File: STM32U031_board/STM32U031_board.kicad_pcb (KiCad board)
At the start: 2 copper layers, 4 parts, among them J3 SWD, J4 UART, J6 QT/ST, U1 STM32U031K8Ux

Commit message: Snapshot:
- after adding L1 inductor package
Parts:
- added C1: 0.1uF, Capacitor_SMD:C_0201_0603Metric, F.Cu at (53.5, 55.5)
- added C2: 47uF, Capacitor_SMD:C_1210_3225Metric, F.Cu at (60.5, 55.5)
- added J1: Conn_01x20, STM32U031_board:Pico_Header_1-20, F.Cu at (43.4, 64.4)
- added J2: Conn_01x20, STM32U031_board:Pico_Header_21-40, F.Cu at (43.4, 46.6)
- added J6: 3.6-15V in, Connector_JST:JST_PH_S2B-PH-SM4-TB_1x02-1MP_P2.00mm_Horizontal, F.Cu at (47.2, 55.5)
- added L1: 33uH, Inductor_SMD:L_Coilcraft_LPS4018, F.Cu at (56.5, 51.0)
- added U2: LTC3336EV#TRMPBF, STM32U031_board:LTC3336EVTRMPBF, F.Cu at (56.5, 55.5)
- J5: renamed from J6; footprint Connector_JST:JST_SH_BM04B-SRSS-TB_1x04-1MP_P1.00mm_Vertical -> Connector_JST:JST_SH_SM04B-SRSS-TB_1x04-1MP_P1.00mm_Horizontal
- moved J4 22.3 mm to (82.5, 51.5), turned to -90 degrees
- moved J3 13.9 mm to (82.5, 59.5), turned to -90 degrees
- moved U1 7.61 mm to (67.4, 55.5)
- moved J5 5.55 mm to (90.0, 55.5), turned to 90 degrees
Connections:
- U1 pad 10: /MCU/PA4 -> /Headers/PA4
- U1 pad 11: /MCU/PA5 -> /Headers/PA5
- U1 pad 12: /MCU/PA6 -> /Headers/PA6
- U1 pad 13: /MCU/PA7 -> /Headers/PA7
- U1 pad 14: /MCU/PB0 -> /Headers/PB0
- U1 pad 15: /MCU/PB1 -> /Headers/PB1
- U1 pad 18: /MCU/PA8 -> /Headers/PA8
- U1 pad 19: /MCU/PA9/TX -> /Connectors, LEDs, pushbutton/PA9/TX
- U1 pad 2: /MCU/PC14 -> /Headers/PC14
- U1 pad 20: /MCU/PA10/RX -> /Connectors, LEDs, pushbutton/PA10/RX
- U1 pad 21: /MCU/PA11 -> /Headers/PA11
- U1 pad 22: /MCU/PA12 -> /Headers/PA12
- U1 pad 23: /MCU/PA13/SWDIO -> /Connectors, LEDs, pushbutton/PA13/SWDIO
- U1 pad 24: /MCU/PA14/SWCLK -> /Connectors, LEDs, pushbutton/PA14/SWCLK
- U1 pad 25: /MCU/PA15 -> /Headers/PA15
- U1 pad 26: /MCU/PB3 -> /Headers/PB3
- U1 pad 27: /MCU/PB4 -> /Headers/PB4
- U1 pad 28: /MCU/PB5 -> /Headers/PB5
- U1 pad 29: /MCU/PB6/SCL -> /Connectors, LEDs, pushbutton/PB6/SCL
- U1 pad 3: /MCU/PC15 -> /Headers/PC15
- U1 pad 30: /MCU/PB7/SDA -> /Connectors, LEDs, pushbutton/PB7/SDA
- U1 pad 31: /MCU/PF3 -> /Connectors, LEDs, pushbutton/PF3
- U1 pad 4: /MCU/PF2 -> /Headers/PF2
- U1 pad 6: /MCU/PA0 -> /Headers/PA0
- U1 pad 7: /MCU/PA1 -> /Headers/PA1
- U1 pad 8: /MCU/PA2 -> /Headers/PA2
- U1 pad 9: /MCU/PA3 -> /Headers/PA3
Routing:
- net /Headers/PB0: track 0.00 -> 35.0 mm, vias 0 -> 4
- net /Headers/PB1: track 0.00 -> 31.9 mm, vias 0 -> 4
- net /Connectors, LEDs, pushbutton/PB7/SDA: track 0.00 -> 30.9 mm, vias 0 -> 1
- net /Connectors, LEDs, pushbutton/PB6/SCL: track 0.00 -> 29.6 mm, vias 0 -> 1
- net /Connectors, LEDs, pushbutton/PA14/SWCLK: track 0.00 -> 29.4 mm
- net /Headers/PA15: track 0.00 -> 28.8 mm
- net /Connectors, LEDs, pushbutton/PA10/RX: track 0.00 -> 26.6 mm, vias 0 -> 2
- net /Headers/PA0: track 0.00 -> 26.5 mm
- net /Connectors, LEDs, pushbutton/PA9/TX: track 0.00 -> 25.9 mm, vias 0 -> 2
- net /Headers/PA1: track 0.00 -> 24.0 mm
- net /Connectors, LEDs, pushbutton/PA13/SWDIO: track 0.00 -> 23.2 mm
- net /Headers/PA2: track 0.00 -> 19.0 mm
- net /Headers/PB3: track 0.00 -> 18.9 mm
- net /Headers/PB4: track 0.00 -> 16.9 mm
- net /Headers/PA12: track 0.00 -> 16.7 mm
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- added copper zone on B.Cu, net GND
- added copper zone on F.Cu, net GND
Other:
- board outline added: 51 x 21 mm

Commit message: Checkin prior to PSU change.
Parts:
- added C3: 100nF, Capacitor_SMD:C_0402_1005Metric, F.Cu at (65.1, 51.9)
- added C4: 100nF, Capacitor_SMD:C_0402_1005Metric, F.Cu at (69.7, 59.1)
- moved L1 0.50 mm to (57.0, 51.0)
- moved J5 0.35 mm to (89.7, 55.5)
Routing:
- net +3.3V: track 15.7 -> 70.3 mm, vias 0 -> 4
- net VSYS: track 0.00 -> 13.5 mm
- net Net-(U2-SW): track 0.00 -> 4.02 mm
- net /Headers/PF2: track 11.8 -> 15.1 mm
- net /Headers/PA12: track 16.7 -> 18.8 mm
- net /Connectors, LEDs, pushbutton/PA14/SWCLK: track 29.4 -> 30.4 mm
- net /Headers/PA15: track 28.8 -> 29.7 mm
- net /Connectors, LEDs, pushbutton/PB6/SCL: track 29.6 -> 30.5 mm
- net GND: track 10.4 -> 9.59 mm
- net /Connectors, LEDs, pushbutton/PA10/RX: track 26.6 -> 25.8 mm
- net /Connectors, LEDs, pushbutton/PB7/SDA: track 30.9 -> 31.5 mm
- net /Headers/PA11: track 14.0 -> 14.5 mm
- net /Headers/PA2: track 19.0 -> 19.1 mm, vias 0 -> 1
- net /Headers/PA0: track 26.5 -> 26.6 mm, vias 0 -> 1
- net /Headers/PA1: vias 0 -> 1
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
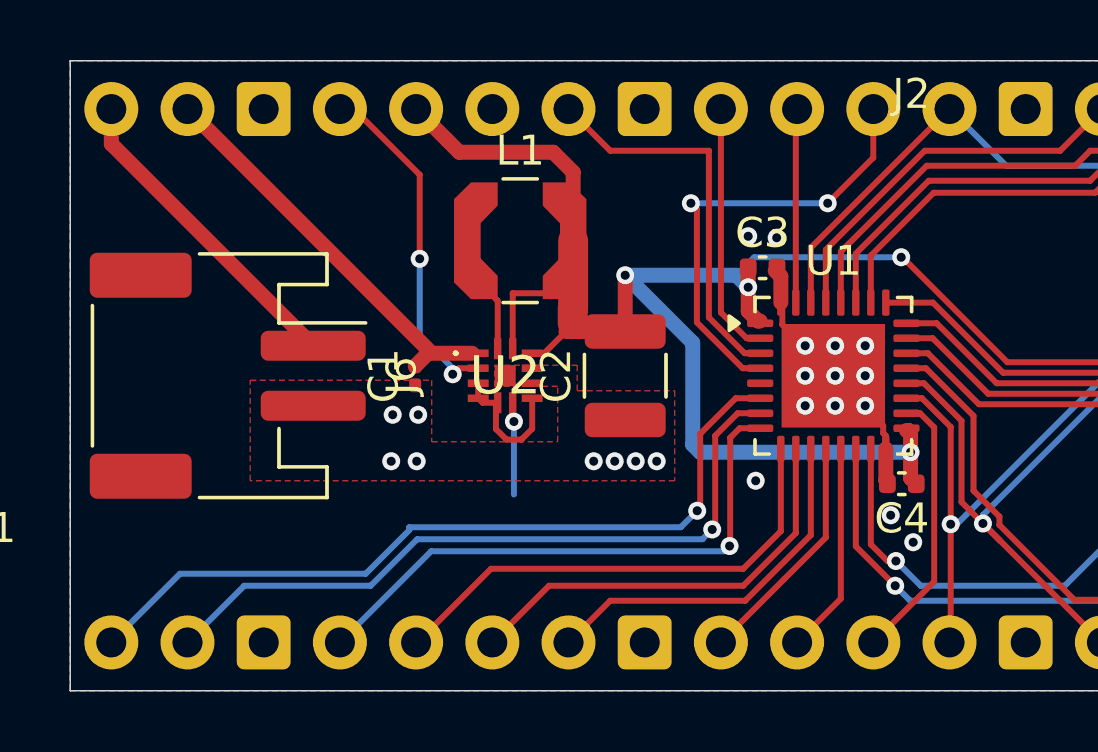
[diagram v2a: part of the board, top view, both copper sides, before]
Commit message: Removed LTC3336, added TPSM365R6.
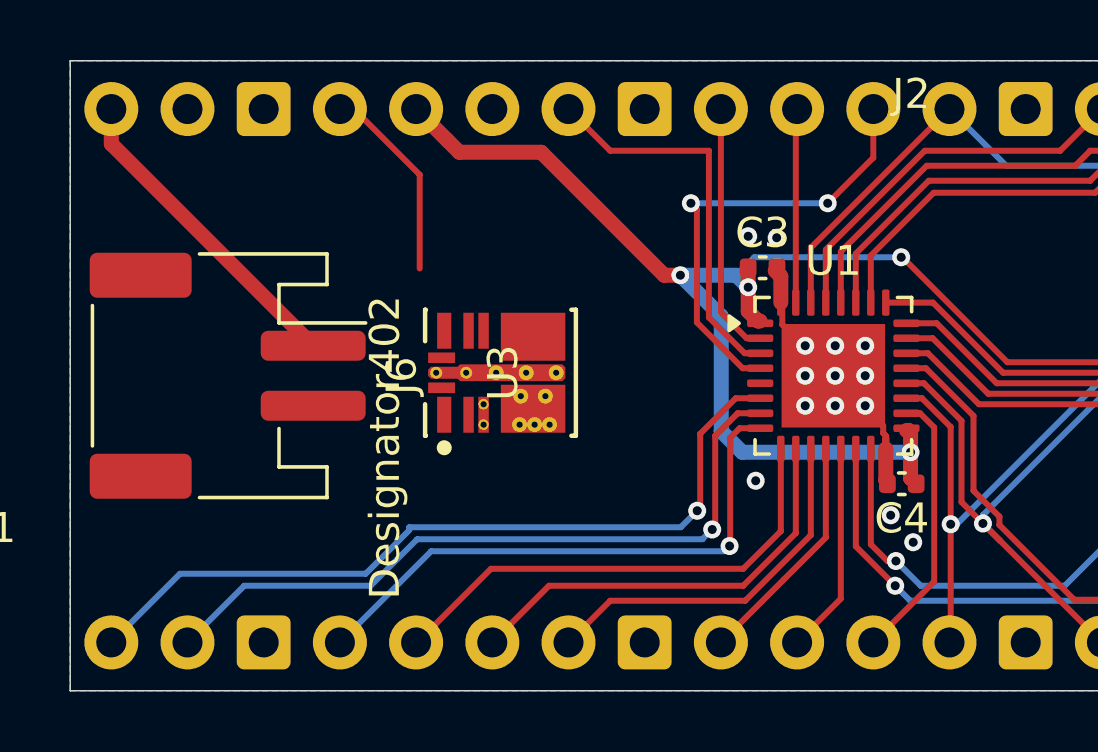
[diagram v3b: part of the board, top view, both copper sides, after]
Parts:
- removed C1: 0.1uF, Capacitor_SMD:C_0201_0603Metric
- removed C2: 47uF, Capacitor_SMD:C_1210_3225Metric
- removed L1: 33uH, Inductor_SMD:L_Coilcraft_LPS4018
- removed U2: LTC3336EV#TRMPBF, STM32U031_board:LTC3336EVTRMPBF
- added U3: TPSM365R6V3RDNR, STM32U031_board:RDN0011A-MFG, F.Cu at (56.4, 55.4)
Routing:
- net +3.3V: track 70.3 -> 55.5 mm
- net VSYS: track 13.5 -> 0.00 mm
- net /Headers/EN: track 11.6 -> 6.69 mm, vias 2 -> 0
- net Net-(U2-INTVCC): track 4.84 -> 0.00 mm
- net Net-(U2-SW): track 4.02 -> 0.00 mm
- net /Power supply/PGOOD: track 3.08 -> 0.00 mm, vias 1 -> 0
- net GND: track 9.59 -> 8.88 mm, vias 22 -> 14

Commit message: Changes before changing PSU again:
- old = TPSM365R6
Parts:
- added C1: 22uF, Capacitor_SMD:C_1210_3225Metric, F.Cu at (57.7, 52.4)
- added C2: 22uF, Capacitor_SMD:C_1210_3225Metric, F.Cu at (60.9, 52.4)
- added C5: 0.1uF, Capacitor_SMD:C_0603_1608Metric, F.Cu at (53.8, 55.5)
- added C6: 2.2uF, Capacitor_SMD:C_1210_3225Metric, F.Cu at (54.6, 57.9)
- added C7: 1uF, Capacitor_SMD:C_0603_1608Metric, F.Cu at (52.7, 49.2)
- moved U2 4.12 mm to (53.7, 52.4)
- moved J6 1.15 mm to (47.2, 56.6)
- renumbered U3 to U2
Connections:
- U2 pad 19: GND -> (no net)
- U2 pad 20: GND -> (no net)
- U2 pad 21: GND -> (no net)
- U2 pad 22: GND -> (no net)
- U2 pad 23: GND -> (no net)
- U2 pad 4: unconnected-(U3-VOUT-Pad4) -> +3.3V
- U2 pad 5: unconnected-(U3-SW-Pad5) -> GND
- U2 pad 6: unconnected-(U3-SW-Pad6) -> GND
- U2 pad 8: unconnected-(U3-VCC-Pad8) -> Net-(U2-VCC)
- U2 pad 9: unconnected-(U3-BIAS-Pad9) -> +3.3V
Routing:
- net VSYS: track 0.00 -> 13.9 mm
- net VBAT: track 10.7 -> 22.5 mm
- net +3.3V: track 55.5 -> 66.3 mm
- net /Headers/EN: track 6.69 -> 11.4 mm
- net /Power supply/PGOOD: track 0.00 -> 4.64 mm, vias 0 -> 1
- net Net-(U2-VCC): track 0.00 -> 1.79 mm
- net /Headers/PF2: track 15.1 -> 16.3 mm
- net GND: vias 14 -> 36
- added copper zone on B.Cu, net +3.3V
- added copper zone on F.Cu, net +3.3V
- added copper zone on B.Cu, net VSYS
- added copper zone on F.Cu, net VSYS
